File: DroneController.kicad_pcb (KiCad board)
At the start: 4 copper layers, 50.7 x 56.1 mm, 54 parts, among them J1 Connector, J2 Connector, J3 Connector, P1 USB_C_Plug, Q2 AO3400A, SW1 SW_SPDT, U2 W25Q16JVSS, U3 BMP280, U4 MPU-6500, U6 L86-M33, U7 915MHz, U9 AP7361C-33E, X1 X322512MSB4SI

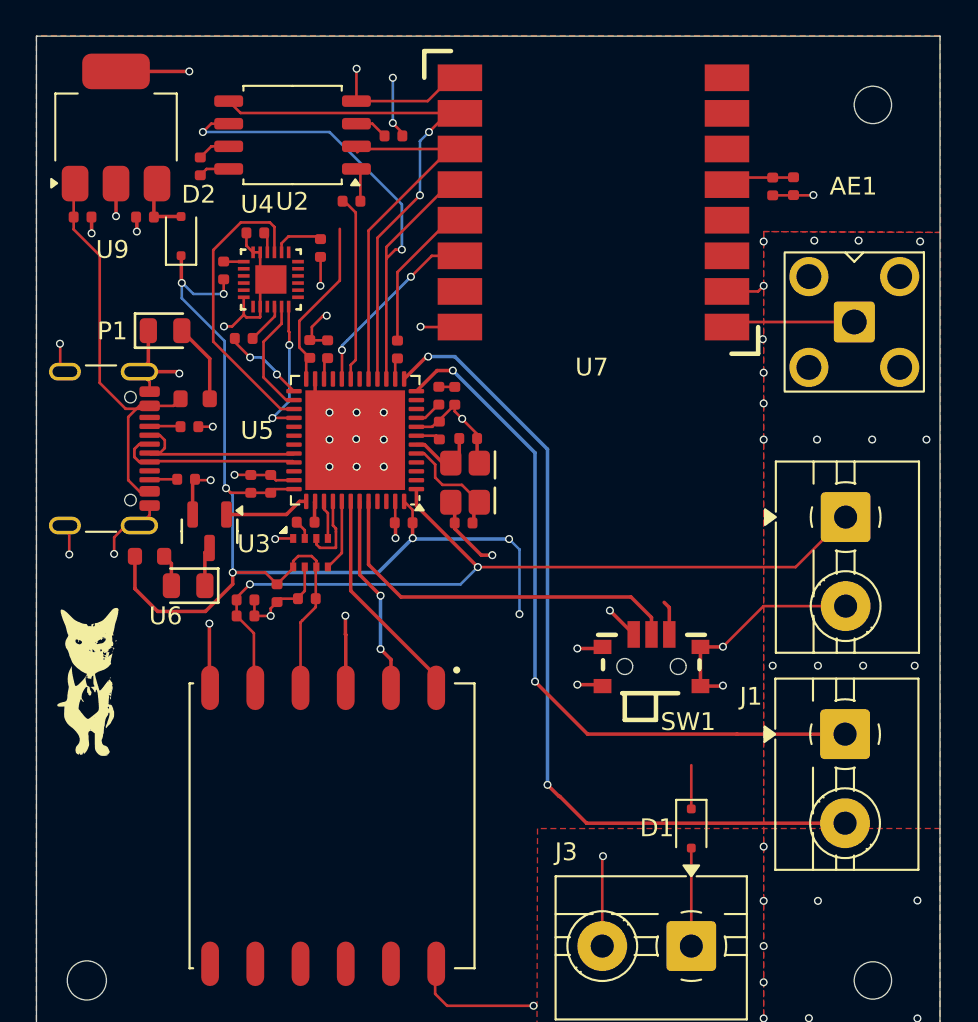
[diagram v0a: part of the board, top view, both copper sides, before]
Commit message: DroneController: Improved clarity of silkscreen and added manual reset test pad for the MCU.
ESC Board: Modified Buck Converter, added SWD debugging, added ICs for BLDC control
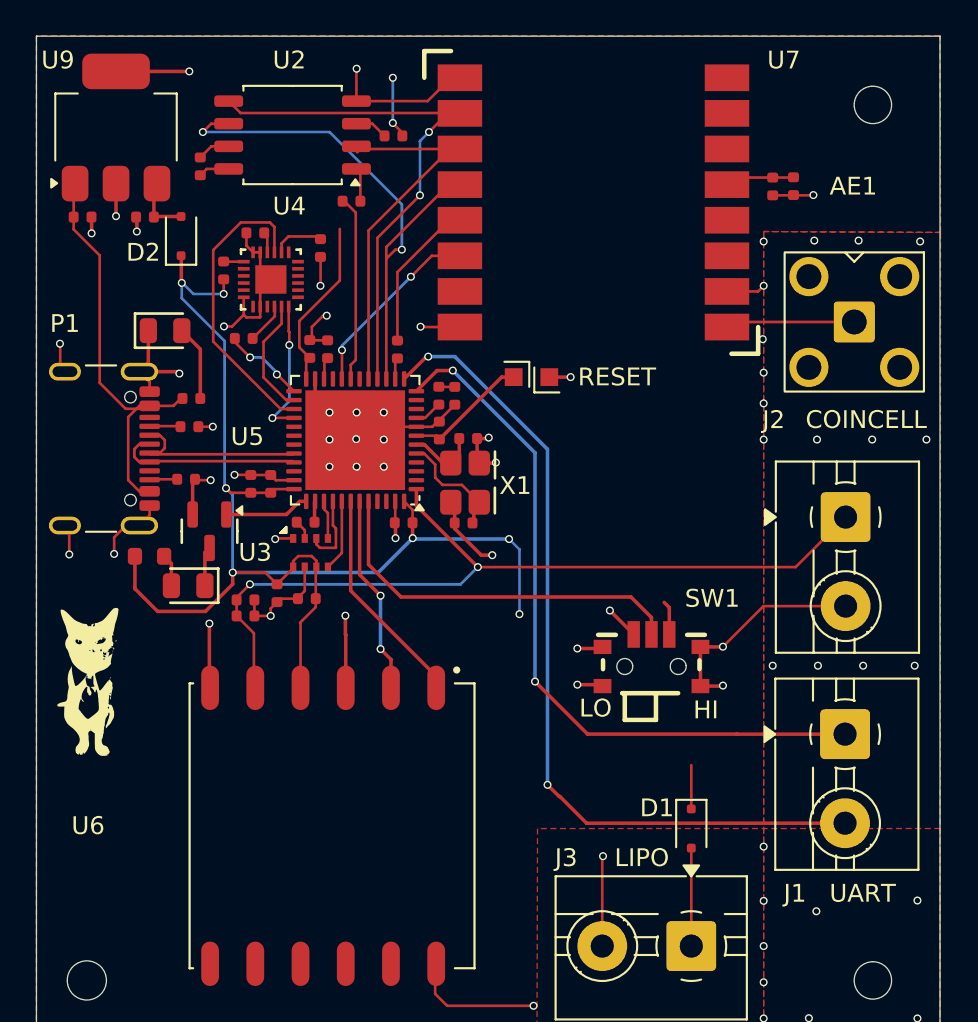
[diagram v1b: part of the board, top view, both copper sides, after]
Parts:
- removed R6: 75Ω, PCM_JLCPCB:R_0603
- added R11: 200Ω, PCM_JLCPCB:R_0402, F.Cu at (110.1, 125.2)
- added REF**: TestPoint_Pad_1.0x1.0mm, TestPoint:TestPoint_Pad_1.0x1.0mm, F.Cu at (128.2, 124.0)
- added REF**: TestPoint_Pad_1.0x1.0mm, TestPoint:TestPoint_Pad_1.0x1.0mm, F.Cu at (130.2, 124.0)
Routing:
- net Net-(U5-NRST): track 1.31 -> 6.94 mm
- net GND: track 119.1 -> 121.6 mm, vias 65 -> 67
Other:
- board text added: "COINCELL"
- board text added: "HI"
- board text added: "J2"
- board text added: "LIPO"
- board text added: "LO"
- board text added: "UART"
- board text added: "X1"

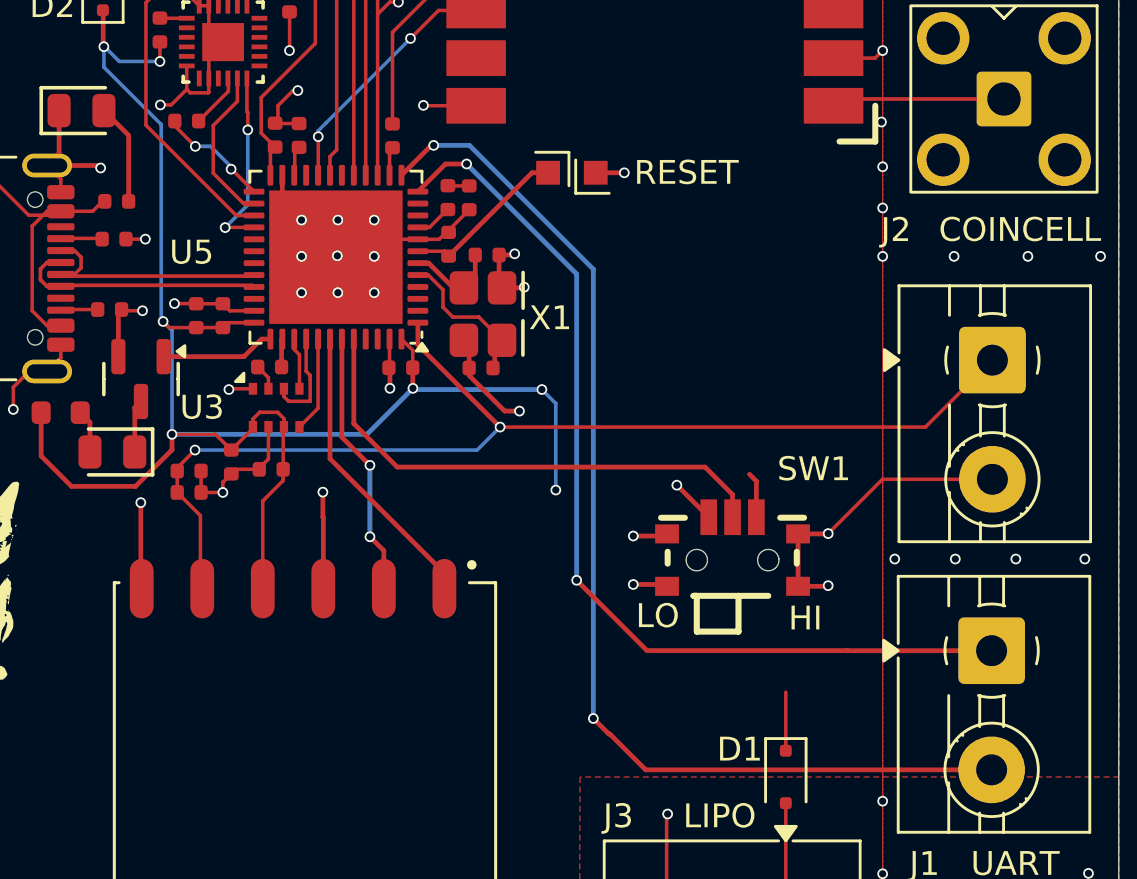
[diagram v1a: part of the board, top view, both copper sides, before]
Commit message: Added UART debugging for DroneController, repecced crystal oscillator.
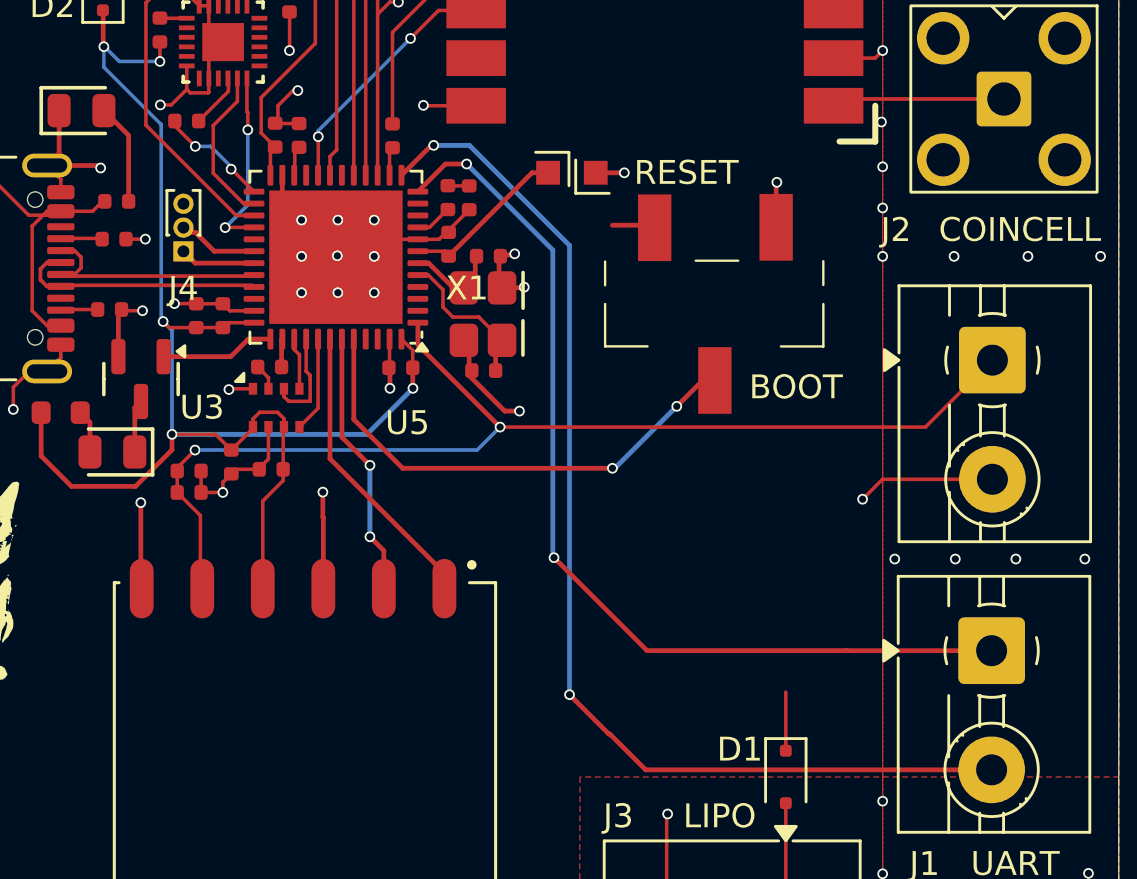
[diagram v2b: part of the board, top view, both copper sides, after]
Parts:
- removed C10: 10pF, PCM_JLCPCB:C_0402
- removed SW1: SW_SPDT, Switches:SW-SMD_MSK12CO2
- added C4: 30pF, PCM_JLCPCB:C_0402, F.Cu at (125.5, 132.3)
- added J4: UART Flash, Connector_PinHeader_1.00mm:PinHeader_1x03_P1.00mm_Vertical, F.Cu at (112.9, 127.3)
- added SHOUHAN-SPDT: SPDT, SW-SHOUHAN_MST-22D18G23J_C2875122:SPDT, F.Cu at (135.2, 129.5)
- C7: value 10pF -> 30pF
- moved C7 0.07 mm to (125.7, 127.5), turned to 180 degrees
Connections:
- C7 pad 1: Net-(U5-PH1-OSC_OUT) -> GND
- C7 pad 2: GND -> Net-(U5-PH1-OSC_OUT)
- U5 pad 30: unconnected-(U5-PA9-Pad30) -> /RX debug 
- U5 pad 31: unconnected-(U5-PA10-Pad31) -> /TX debug 
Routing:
- net +3.3V: track 98.2 -> 88.1 mm, vias 9 -> 7
- net GND: track 121.6 -> 111.9 mm, vias 67 -> 64
- net /RX debug : track 0.00 -> 3.09 mm
- net /TX debug : track 0.00 -> 2.88 mm
- net Net-(SW2-B): track 21.6 -> 20.9 mm, vias 0 -> 2
- net Net-(U5-PH0-OSC_IN): track 6.41 -> 7.01 mm
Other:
- board text added: "BOOT"
- board text removed: "HI"
- board text removed: "LO"

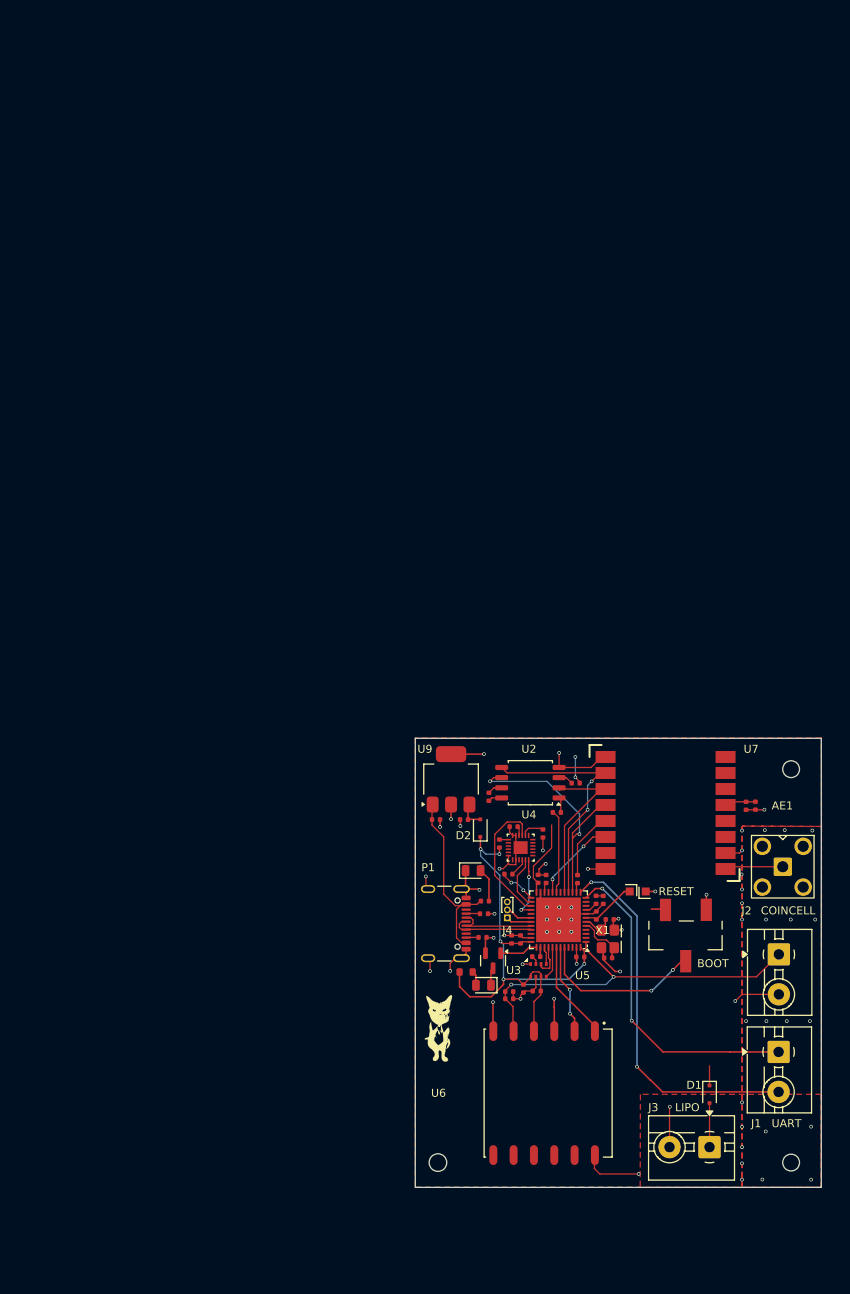
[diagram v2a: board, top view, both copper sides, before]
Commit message: Fixed wiring, Added pull-up on CS, respecced IMU, began work on a new layout
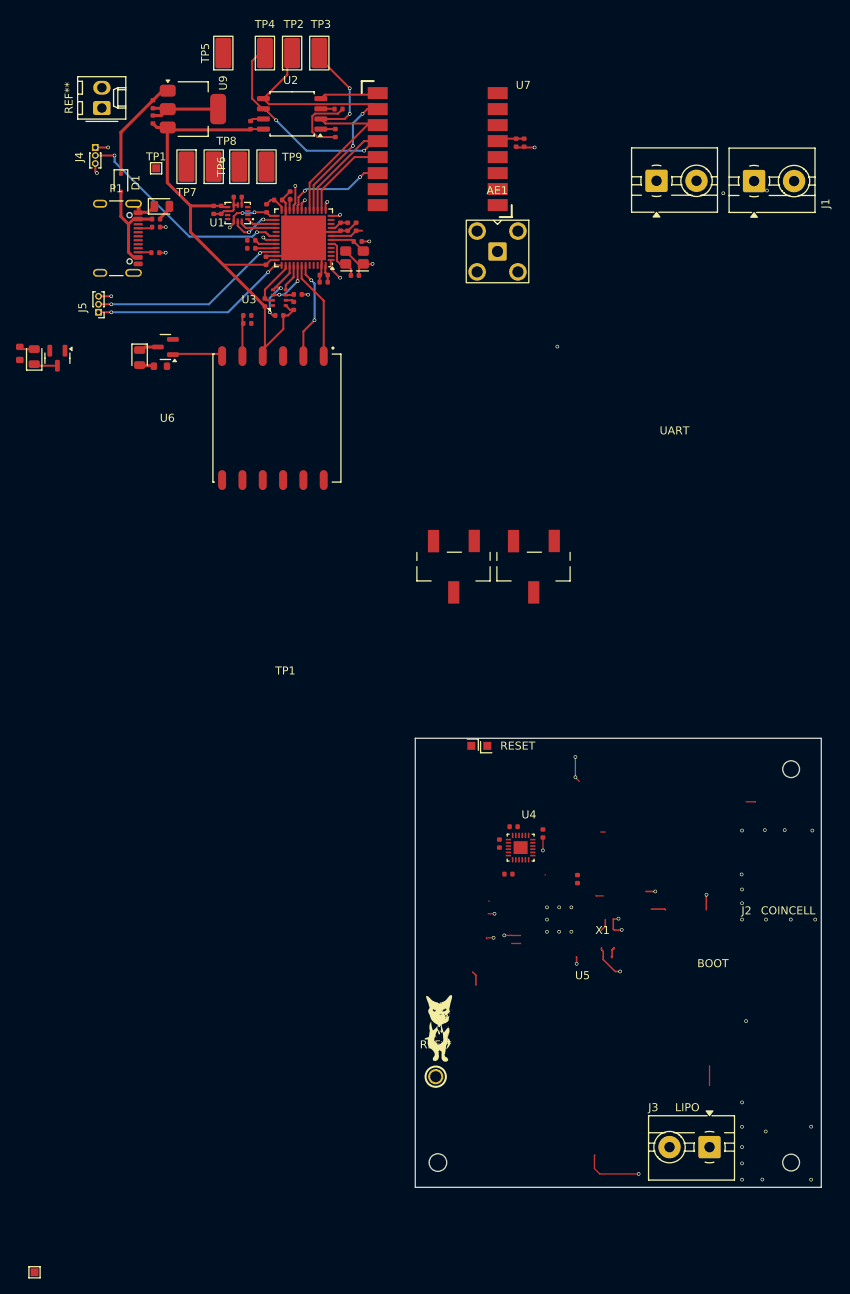
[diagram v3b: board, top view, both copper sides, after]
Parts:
- removed D2: PMEG3015EJ, Diode_SMD:D_SOD-323F
- removed R8: 5.1kΩ, PCM_JLCPCB:R_0402
- added C10: 20pF, PCM_JLCPCB:C_0402, F.Cu at (93.8, 47.0)
- added C11: 20pF, PCM_JLCPCB:C_0402, F.Cu at (94.2, 42.8)
- added C14: 10uF, PCM_JLCPCB:C_0402, F.Cu at (114.0, 30.4)
- added D6: Red, PCM_JLCPCB:D_0805, F.Cu at (66.9, 57.3)
- added J5: UART Flash, Connector_PinHeader_1.00mm:PinHeader_1x03_P1.00mm_Vertical, F.Cu at (61.8, 51.6)
- added Q3: AO3400A, PCM_JLCPCB:Q_SOT-23, F.Cu at (70.2, 55.9)
- added R12: 5.1kΩ, PCM_JLCPCB:R_0402, F.Cu at (82.8, 38.6)
- added R13: 75Ω, PCM_JLCPCB:R_0603, F.Cu at (69.5, 58.3)
- added R14: 22Ω, PCM_JLCPCB:R_0402, F.Cu at (80.9, 43.6)
- added R15: 5.1kΩ, PCM_JLCPCB:R_0402, F.Cu at (84.4, 52.0)
- added R6: 22Ω, PCM_JLCPCB:R_0402, F.Cu at (80.9, 42.6)
- added R9: 5.1kΩ, PCM_JLCPCB:R_0402, F.Cu at (82.6, 50.4)
- added REF**: Molex_KK-254_AE-6410-02A_1x02_P2.54mm_Vertical, Connector_Molex:Molex_KK-254_AE-6410-02A_1x02_P2.54mm_Vertical, F.Cu at (62.2, 26.1)
- added REF**: TEST-TH_BD2.54-P1.4_BLACK, easyeda2kicad:TEST-TH_BD2.54-P1.4_BLACK, F.Cu at (104.0, 147.2)
- added SHOUHAN-SPDT: SPDT, SW-SHOUHAN_MST-22D18G23J_C2875122:SPDT, F.Cu at (116.2, 83.4)
- added TP1: TestPoint, TestPoint:TestPoint_Pad_1.0x1.0mm, F.Cu at (53.8, 171.6)
- added TP1: TestPoint, TestPoint:TestPoint_Pad_1.0x1.0mm, F.Cu at (69.0, 33.6)
- added TP2: TestPoint, TestPoint:TestPoint_Keystone_5019_Miniature, F.Cu at (86.0, 19.2)
- added TP3: TestPoint, TestPoint:TestPoint_Keystone_5019_Miniature, F.Cu at (89.4, 19.2)
- added TP4: TestPoint, TestPoint:TestPoint_Keystone_5019_Miniature, F.Cu at (82.6, 19.2)
- added TP5: TestPoint, TestPoint:TestPoint_Keystone_5019_Miniature, F.Cu at (77.4, 19.2)
- added TP6: TestPoint, TestPoint:TestPoint_Keystone_5019_Miniature, F.Cu at (79.4, 33.4)
- added TP7: TestPoint, TestPoint:TestPoint_Keystone_5019_Miniature, F.Cu at (72.8, 33.4)
- added TP8: TestPoint, TestPoint:TestPoint_Keystone_5019_Miniature, F.Cu at (76.2, 33.4)
- added TP9: TestPoint, TestPoint:TestPoint_Keystone_5019_Miniature, F.Cu at (82.8, 33.4)
- added U1: ICM-42605, easyeda2kicad:LGA-14_L3.0-W2.5-P0.50-TL, F.Cu at (79.2, 39.2)
- C4: value 30pF -> 4.7uF
- C5: value 10uF -> 4.7uF
- C6: value 10uF -> 100nF
- C7: value 30pF -> 2.2uF
- C8: value 10uF -> 10nF
- U5: value ~ -> STM32F411
- X1: value X322512MSB4SI -> Shenzhen SCTF Elec SX2B12.000F1010F30
- moved D1 135.6 mm to (64.6, 35.4)
- moved C4 119.3 mm to (68.6, 27.5), turned to 90 degrees
- moved C5 114.8 mm to (68.6, 25.6)
- moved J4 109.2 mm to (61.4, 31.0), turned to 0 degrees
- moved J1 108.9 mm to (143.7, 35.2), turned to 0 degrees
- moved C7 101.6 mm to (76.2, 38.8), turned to -90 degrees
- moved J2 97.9 mm to (131.6, 35.2), turned to 0 degrees
- moved D5 96.6 mm to (53.8, 57.1), turned to 90 degrees
- moved C29 95.5 mm to (82.7, 45.2), turned to -90 degrees
- moved R5 95.4 mm to (52.0, 56.7), turned to 90 degrees
- moved R1 95.1 mm to (69.0, 41.0)
- moved P1 95.0 mm to (63.1, 42.4)
- moved R2 94.9 mm to (68.9, 44.1)
- moved R11 94.6 mm to (69.0, 40.0)
- moved Q2 92.9 mm to (56.7, 57.3)
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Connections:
- net /RX debug  renamed /Debug_TX
- net Net-(Q2-G) renamed /SWCLK
- C20 pad 1: VDD -> 3.3V
- C20 pad 2: Net-(C20-Pad2) -> GND
- C21 pad 1: Net-(C20-Pad2) -> 3.3V
- C4 pad 1: Net-(U5-PH0-OSC_IN) -> +3.3V
- C5 pad 1: +3.3V -> Net-(D1-K)
- C6 pad 1: Net-(D2-A) -> GND
- C6 pad 2: GND -> +3.3V
- C7 pad 1: GND -> +3.3V
- C7 pad 2: Net-(U5-PH1-OSC_OUT) -> GND
- C8 pad 1: +5V -> GND
- C8 pad 2: GND -> +3.3V
- D1 pad 1: +3.3V -> Net-(D1-K)
- D1 pad 2: /LIPO_3.3V -> +5V
- J3 pad 1: /LIPO_3.3V -> +3.3V
- J4 pad 1: /TX debug  -> GND
- J4 pad 3: GND -> /Debug_RX
- P1 pad A6: /USB_FS_DP -> unconnected-(P1-DP1-PadA6)
- P1 pad B7: /USB_FS_DN -> unconnected-(P1-DN2-PadB7)
- R10 pad 1: /SPI1_NSS -> +3.3V
- R10 pad 2: Net-(U7-NSS) -> /SPI1_NSS
- R7 pad 2: Net-(U2-~{CS}) -> +3.3V
- U2 pad 1: Net-(U2-~{CS}) -> /SPI5_NSS
- U3 pad 2: Net-(U3-CSB) -> /SPI3_NSS
- U3 pad 3: /SPI3_MISO -> /SPI3_MOSI
- U3 pad 5: /SPI3_MOSI -> /SPI3_MISO
- U5 pad 11: unconnected-(U5-PA1-Pad11) -> /ADC1
- U5 pad 21: unconnected-(U5-PB10-Pad21) -> /IMU_INT
- U5 pad 31: /TX debug  -> /Debug_RX
- U5 pad 32: /USB_FS_DN -> Net-(U5-PA11)
- U5 pad 33: /USB_FS_DP -> Net-(U5-PA12)
- U5 pad 34: unconnected-(U5-PA13-Pad34) -> /SWDIO
- U5 pad 9: VDD -> 3.3V
- U6 pad 10: unconnected-(U6-~{RESET}-Pad10) -> Net-(U6-~{RESET})
- U6 pad 6: GND -> Net-(Q3-G)
- U7 pad 5: Net-(U7-NSS) -> /SPI1_NSS
- U9 pad 1: +5V -> Net-(D1-K)
- U9 pad 3: Net-(D2-A) -> +3.3V
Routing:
- net /MCU_RX2: track 47.2 -> 1.15 mm
- net +BATT: track 47.5 -> 7.83 mm, vias 2 -> 1
- net /MCU_TX2: track 40.5 -> 1.19 mm
- net /SWDIO: track 0.00 -> 24.9 mm, vias 0 -> 2
- net /Debug_TX: track 3.09 -> 27.6 mm, vias 0 -> 2
- net Net-(SW2-B): track 20.9 -> 0.00 mm, vias 2 -> 0
- net /SWCLK: track 4.78 -> 25.3 mm, vias 0 -> 2
- net GND: track 111.9 -> 92.0 mm, vias 64 -> 48
- net /SPI1_MOSI: track 21.2 -> 35.7 mm, vias 0 -> 2
- net Net-(D1-K): track 0.00 -> 13.8 mm
- net +3.3V: track 88.1 -> 101.4 mm, vias 7 -> 2
- net /SPI2_MISO: track 16.9 -> 3.79 mm
- net +5V: track 23.7 -> 12.7 mm
- net /USB_FS_DN: track 10.6 -> 0.00 mm
- net /USB_FS_DP: track 10.5 -> 0.00 mm
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- removed copper zone on F.Cu, net +3.3V
- removed copper zone on F.Cu, net GND
